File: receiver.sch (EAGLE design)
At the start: 29 parts

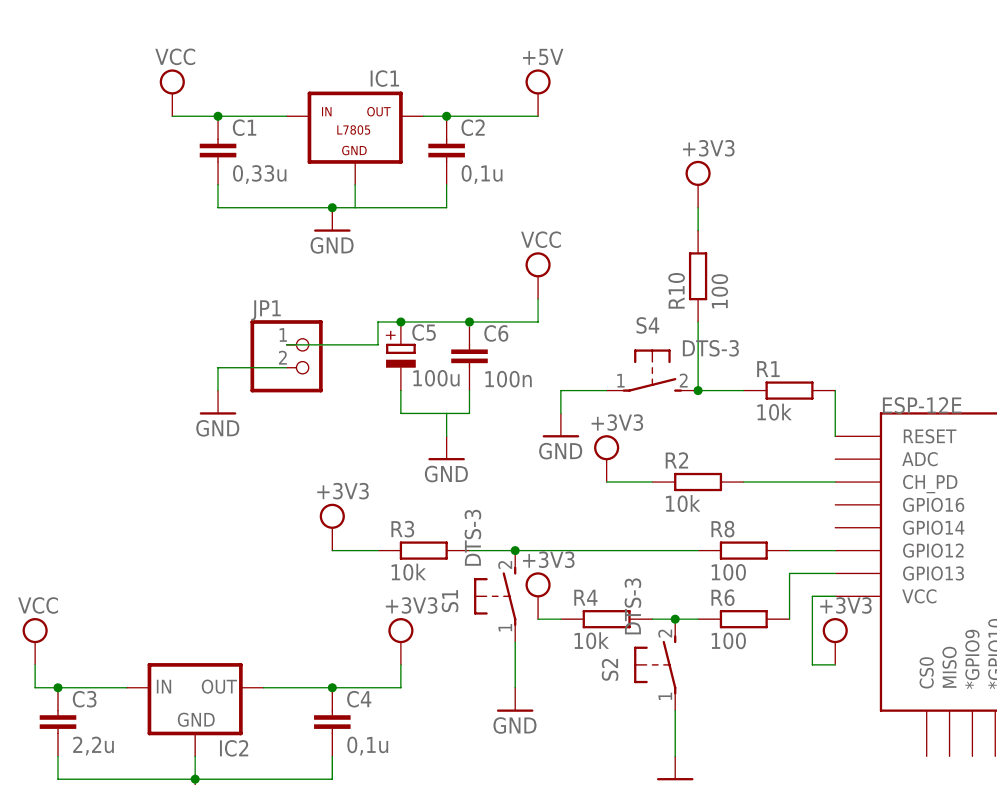
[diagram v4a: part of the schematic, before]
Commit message: Changed 5V LCD on 3,3V LCd, replaced 5V from schematic on 3,3V.
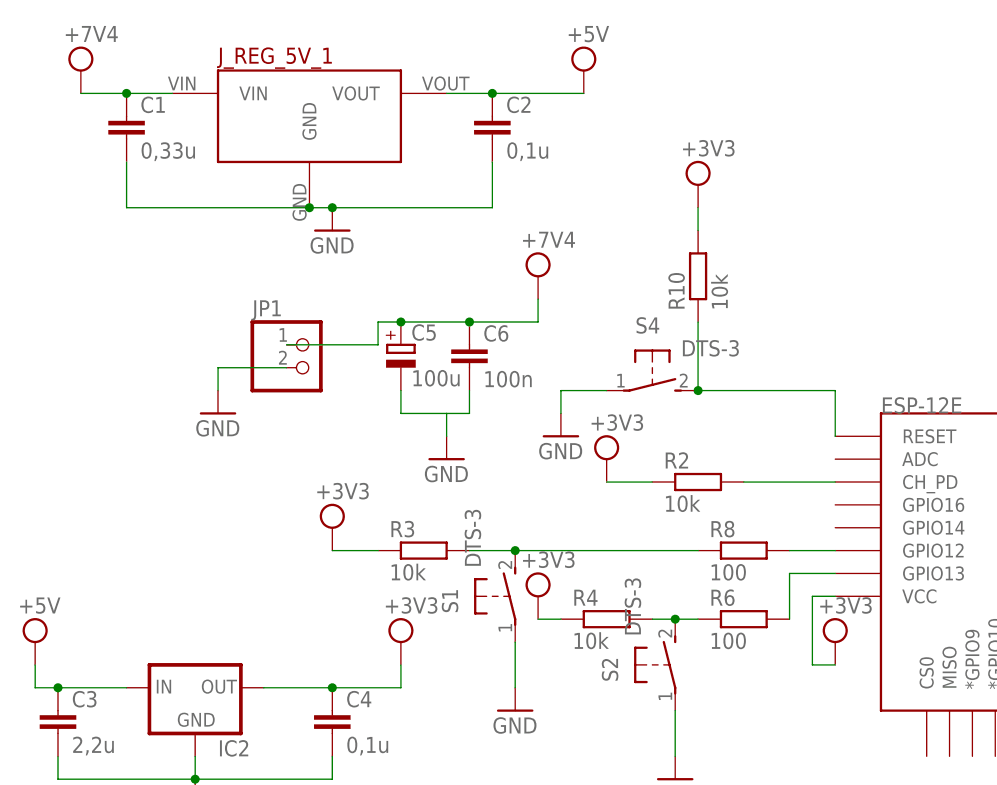
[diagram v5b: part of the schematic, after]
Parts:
- removed IC1: (no value), tango:L7805
- removed R1: 10k, rcl:R-EU_0204/5
- added J_REG_5V_1: 5V_VOLTAGE_REGULATOR, Pololu Voltage Regulators:5V_VOLTAGE_REGULATOR
- R10: value 100 -> 10k
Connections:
- removed net N$12: R1.1, R10.1, S4.2
- net GND: now also J_REG_5V_1.GND; no longer IC1.GND
- net N$1: now also R10.1, S4.2; no longer R1.2
- net VCC: now also J_REG_5V_1.VIN, J_REG_5V_1.VOUT; no longer IC1.IN, IC1.OUT
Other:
- moved on the sheet: C1, C2
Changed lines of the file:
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@@
 <part name="ESP-12E" library="esp8266modules" deviceset="ESP12E" device="SMD"/>
 <part name="GND1" library="supply1" library_urn="urn:adsk.eagle:library:371" deviceset="GND" device=""/>
-<part name="R1" library="rcl" library_urn="urn:adsk.eagle:library:334" deviceset="R-EU_" device="0204/5" package3d_urn="urn:adsk.eagle:package:23488/1" value="10k"/>
 <part name="R2" library="rcl" library_urn="urn:adsk.eagle:library:334" deviceset="R-EU_" device="0204/5" package3d_urn="urn:adsk.eagle:package:23488/1" value="10k"/>
 <part name="LCD" library="pinhead" library_urn="urn:adsk.eagle:library:325" deviceset="PINHD-1X4" device="" package3d_urn="urn:adsk.eagle:package:22407/2"/>
@@
 <part name="R4" library="rcl" library_urn="urn:adsk.eagle:library:334" deviceset="R-EU_" device="0204/5" package3d_urn="urn:adsk.eagle:package:23488/1" value="10k"/>
 <part name="R5" library="rcl" library_urn="urn:adsk.eagle:library:334" deviceset="R-EU_" device="0204/5" package3d_urn="urn:adsk.eagle:package:23488/1" value="10k"/>
-<part name="IC1" library="tango" deviceset="L7805" device=""/>
 <part name="C1" library="rcl" library_urn="urn:adsk.eagle:library:334" deviceset="C-EU" device="025-025X050" package3d_urn="urn:adsk.eagle:package:23629/2" value="0,33u"/>
 <part name="C2" library="rcl" library_urn="urn:adsk.eagle:library:334" deviceset="C-EU" device="025-025X050" package3d_urn="urn:adsk.eagle:package:23629/2" value="0,1u"/>
@@
 <part name="JP1" library="pinhead" library_urn="urn:adsk.eagle:library:325" deviceset="PINHD-1X2" device="" package3d_urn="urn:adsk.eagle:package:22435/2"/>
 <part name="GND6" library="supply1" library_urn="urn:adsk.eagle:library:371" deviceset="GND" device=""/>
-<part name="SUPPLY9" library="supply2" library_urn="urn:adsk.eagle:library:372" deviceset="VCC" device=""/>
+<part name="SUPPLY9" library="supply2" library_urn="urn:adsk.eagle:library:372" deviceset="VCC" device="" value="+7V4"/>
 <part name="IC2" library="lf33" deviceset="LFXXCV" device="L"/>
 <part name="C3" library="rcl" library_urn="urn:adsk.eagle:library:334" deviceset="C-EU" device="025-025X050" package3d_urn="urn:adsk.eagle:package:23629/2" value="2,2u"/>
 <part name="C4" library="rcl" library_urn="urn:adsk.eagle:library:334" deviceset="C-EU" device="025-025X050" package3d_urn="urn:adsk.eagle:package:23629/2" value="0,1u"/>
 <part name="GND7" library="supply1" library_urn="urn:adsk.eagle:library:371" deviceset="GND" device=""/>
-<part name="SUPPLY10" library="supply2" library_urn="urn:adsk.eagle:library:372" deviceset="VCC" device=""/>
+<part name="SUPPLY10" library="supply2" library_urn="urn:adsk.eagle:library:372" deviceset="VCC" device="" value="+5V"/>
 <part name="R6" library="rcl" library_urn="urn:adsk.eagle:library:334" deviceset="R-EU_" device="0204/5" package3d_urn="urn:adsk.eagle:package:23488/1" value="100"/>
 <part name="C5" library="rcl" library_urn="urn:adsk.eagle:library:334" deviceset="CPOL-EU" device="E2.5-6" package3d_urn="urn:adsk.eagle:package:23349/1" value="100u"/>
 <part name="C6" library="rcl" library_urn="urn:adsk.eagle:library:334" deviceset="C-EU" device="025-025X050" package3d_urn="urn:adsk.eagle:package:23629/2" value="100n"/>
-<part name="SUPPLY3" library="supply2" library_urn="urn:adsk.eagle:library:372" deviceset="VCC" device=""/>
+<part name="SUPPLY3" library="supply2" library_urn="urn:adsk.eagle:library:372" deviceset="VCC" device="" value="+7V4"/>
 <part name="GND8" library="supply1" library_urn="urn:adsk.eagle:library:371" deviceset="GND" device=""/>
 <part name="R7" library="rcl" library_urn="urn:adsk.eagle:library:334" deviceset="R-EU_" device="0204/5" package3d_urn="urn:adsk.eagle:package:23488/1" value="10k"/>
@@
 <part name="SUPPLY16" library="supply2" library_urn="urn:adsk.eagle:library:372" deviceset="VCC" device="" value="+3V3"/>
 <part name="S4" library="switch-tact" deviceset="DTS-3" device=""/>
-<part name="R10" library="rcl" library_urn="urn:adsk.eagle:library:334" deviceset="R-EU_" device="0204/5" package3d_urn="urn:adsk.eagle:package:23488/1" value="100"/>
+<part name="R10" library="rcl" library_urn="urn:adsk.eagle:library:334" deviceset="R-EU_" device="0204/5" package3d_urn="urn:adsk.eagle:package:23488/1" value="10k"/>
 <part name="GND9" library="supply1" library_urn="urn:adsk.eagle:library:371" deviceset="GND" device=""/>
 <part name="R11" library="rcl" library_urn="urn:adsk.eagle:library:334" deviceset="R-EU_" device="0204/5" package3d_urn="urn:adsk.eagle:package:23488/1" value="4,7k"/>
@@
 <part name="SUPPLY17" library="supply2" library_urn="urn:adsk.eagle:library:372" deviceset="VCC" device="" value="+5V"/>
 <part name="SUPPLY18" library="supply2" library_urn="urn:adsk.eagle:library:372" deviceset="VCC" device="" value="+5V"/>
+<part name="J_REG_5V_1" library="Pololu Voltage Regulators" deviceset="5V_VOLTAGE_REGULATOR" device=""/>
 </parts>
 <sheets>
@@
 <instance part="ESP-12E" gate="G$1" x="58.42" y="66.04"/>
 <instance part="GND1" gate="1" x="76.2" y="50.8"/>
-<instance part="R1" gate="G$1" x="35.56" y="78.74"/>
 <instance part="R2" gate="G$1" x="25.4" y="68.58"/>
 <instance part="LCD" gate="A" x="152.4" y="73.66"/>
@@
 <instance part="R4" gate="G$1" x="15.24" y="53.34"/>
 <instance part="R5" gate="G$1" x="91.44" y="35.56"/>
-<instance part="IC1" gate="A" x="-12.7" y="106.68"/>
-<instance part="C1" gate="G$1" x="-27.94" y="106.68"/>
-<instance part="C2" gate="G$1" x="-2.54" y="106.68"/>
+<instance part="C1" gate="G$1" x="-38.1" y="109.22"/>
+<instance part="C2" gate="G$1" x="2.54" y="109.22"/>
 <instance part="GND5" gate="1" x="-15.24" y="96.52"/>
 <instance part="JP1" gate="G$1" x="-17.78" y="81.28"/>
 <instance part="GND6" gate="1" x="-27.94" y="76.2"/>
-<instance part="SUPPLY9" gate="G$1" x="-33.02" y="111.76"/>
+<instance part="SUPPLY9" gate="G$1" x="-43.18" y="114.3"/>
 <instance part="IC2" gate="A" x="-30.48" y="45.72"/>
 <instance part="C3" gate="G$1" x="-45.72" y="43.18"/>
@@
 <instance part="SUPPLY8" gate="G$1" x="25.4" y="101.6"/>
 <instance part="SUPPLY11" gate="G$1" x="15.24" y="71.12"/>
-<instance part="SUPPLY12" gate="G$1" x="7.62" y="111.76"/>
+<instance part="SUPPLY12" gate="G$1" x="12.7" y="114.3"/>
 <instance part="SUPPLY7" gate="G$1" x="142.24" y="86.36"/>
 <instance part="SUPPLY4" gate="G$1" x="-15.24" y="63.5"/>
@@
 <instance part="SUPPLY17" gate="G$1" x="134.62" y="99.06"/>
 <instance part="SUPPLY18" gate="G$1" x="134.62" y="55.88"/>
+<instance part="J_REG_5V_1" gate="J_REG_5V" x="-17.78" y="111.76"/>
 </instances>
 <busses>
@@
 <segment>
 <pinref part="C1" gate="G$1" pin="1"/>
-<pinref part="IC1" gate="A" pin="IN"/>
-<wire x1="-27.94" y1="109.22" x2="-20.32" y2="109.22" width="0.1524" layer="91"/>
-<wire x1="-27.94" y1="109.22" x2="-33.02" y2="109.22" width="0.1524" layer="91"/>
-<junction x="-27.94" y="109.22"/>
+<wire x1="-38.1" y1="111.76" x2="-43.18" y2="111.76" width="0.1524" layer="91"/>
 <pinref part="SUPPLY9" gate="G$1" pin="VCC"/>
+<pinref part="J_REG_5V_1" gate="J_REG_5V" pin="VIN"/>
+<wire x1="-33.02" y1="111.76" x2="-38.1" y2="111.76" width="0.1524" layer="91"/>
+<junction x="-38.1" y="111.76"/>
 </segment>
 <segment>
@@
 </segment>
 <segment>
-<pinref part="IC1" gate="A" pin="OUT"/>
-<wire x1="-5.08" y1="109.22" x2="-2.54" y2="109.22" width="0.1524" layer="91"/>
 <pinref part="C2" gate="G$1" pin="1"/>
-<wire x1="-2.54" y1="109.22" x2="7.62" y2="109.22" width="0.1524" layer="91"/>
-<junction x="-2.54" y="109.22"/>
+<wire x1="2.54" y1="111.76" x2="12.7" y2="111.76" width="0.1524" layer="91"/>
 <pinref part="SUPPLY12" gate="G$1" pin="VCC"/>
+<pinref part="J_REG_5V_1" gate="J_REG_5V" pin="VOUT"/>
+<wire x1="-2.54" y1="111.76" x2="2.54" y2="111.76" width="0.1524" layer="91"/>
+<junction x="2.54" y="111.76"/>
 </segment>
 <segment>
@@
 </segment>
 <segment>
-<pinref part="IC1" gate="A" pin="GND"/>
-<wire x1="-12.7" y1="101.6" x2="-12.7" y2="99.06" width="0.1524" layer="91"/>
-<wire x1="-12.7" y1="99.06" x2="-15.24" y2="99.06" width="0.1524" layer="91"/>
-<wire x1="-15.24" y1="99.06" x2="-27.94" y2="99.06" width="0.1524" layer="91"/>
-<wire x1="-12.7" y1="99.06" x2="-2.54" y2="99.06" width="0.1524" layer="91"/>
+<wire x1="-15.24" y1="99.06" x2="-17.78" y2="99.06" width="0.1524" layer="91"/>
+<wire x1="-17.78" y1="99.06" x2="-38.1" y2="99.06" width="0.1524" layer="91"/>
 <pinref part="C1" gate="G$1" pin="2"/>
-<wire x1="-27.94" y1="101.6" x2="-27.94" y2="99.06" width="0.1524" layer="91"/>
+<wire x1="-38.1" y1="104.14" x2="-38.1" y2="99.06" width="0.1524" layer="91"/>
+<pinref part="GND5" gate="1" pin="GND"/>
+<pinref part="J_REG_5V_1" gate="J_REG_5V" pin="GND"/>
+<junction x="-17.78" y="99.06"/>
 <pinref part="C2" gate="G$1" pin="2"/>
-<wire x1="-2.54" y1="101.6" x2="-2.54" y2="99.06" width="0.1524" layer="91"/>
-<pinref part="GND5" gate="1" pin="GND"/>
+<wire x1="-15.24" y1="99.06" x2="2.54" y2="99.06" width="0.1524" layer="91"/>
+<wire x1="2.54" y1="99.06" x2="2.54" y2="104.14" width="0.1524" layer="91"/>
 <junction x="-15.24" y="99.06"/>
 </segment>
@@
 <segment>
 <pinref part="ESP-12E" gate="G$1" pin="RESET"/>
-<pinref part="R1" gate="G$1" pin="2"/>
 <wire x1="40.64" y1="73.66" x2="40.64" y2="78.74" width="0.1524" layer="91"/>
+<pinref part="R10" gate="G$1" pin="1"/>
+<pinref part="S4" gate="G$1" pin="2"/>
+<wire x1="25.4" y1="86.36" x2="25.4" y2="78.74" width="0.1524" layer="91"/>
+<junction x="25.4" y="78.74"/>
+<wire x1="40.64" y1="78.74" x2="25.4" y2="78.74" width="0.1524" layer="91"/>
 </segment>
 </net>
@@
 </segment>
 </net>
-<net name="N$12" class="0">
-<segment>
-<pinref part="R10" gate="G$1" pin="1"/>
-<pinref part="S4" gate="G$1" pin="2"/>
-<wire x1="25.4" y1="86.36" x2="25.4" y2="78.74" width="0.1524" layer="91"/>
-<pinref part="R1" gate="G$1" pin="1"/>
-<wire x1="25.4" y1="78.74" x2="30.48" y2="78.74" width="0.1524" layer="91"/>
-<junction x="25.4" y="78.74"/>
-</segment>
-</net>

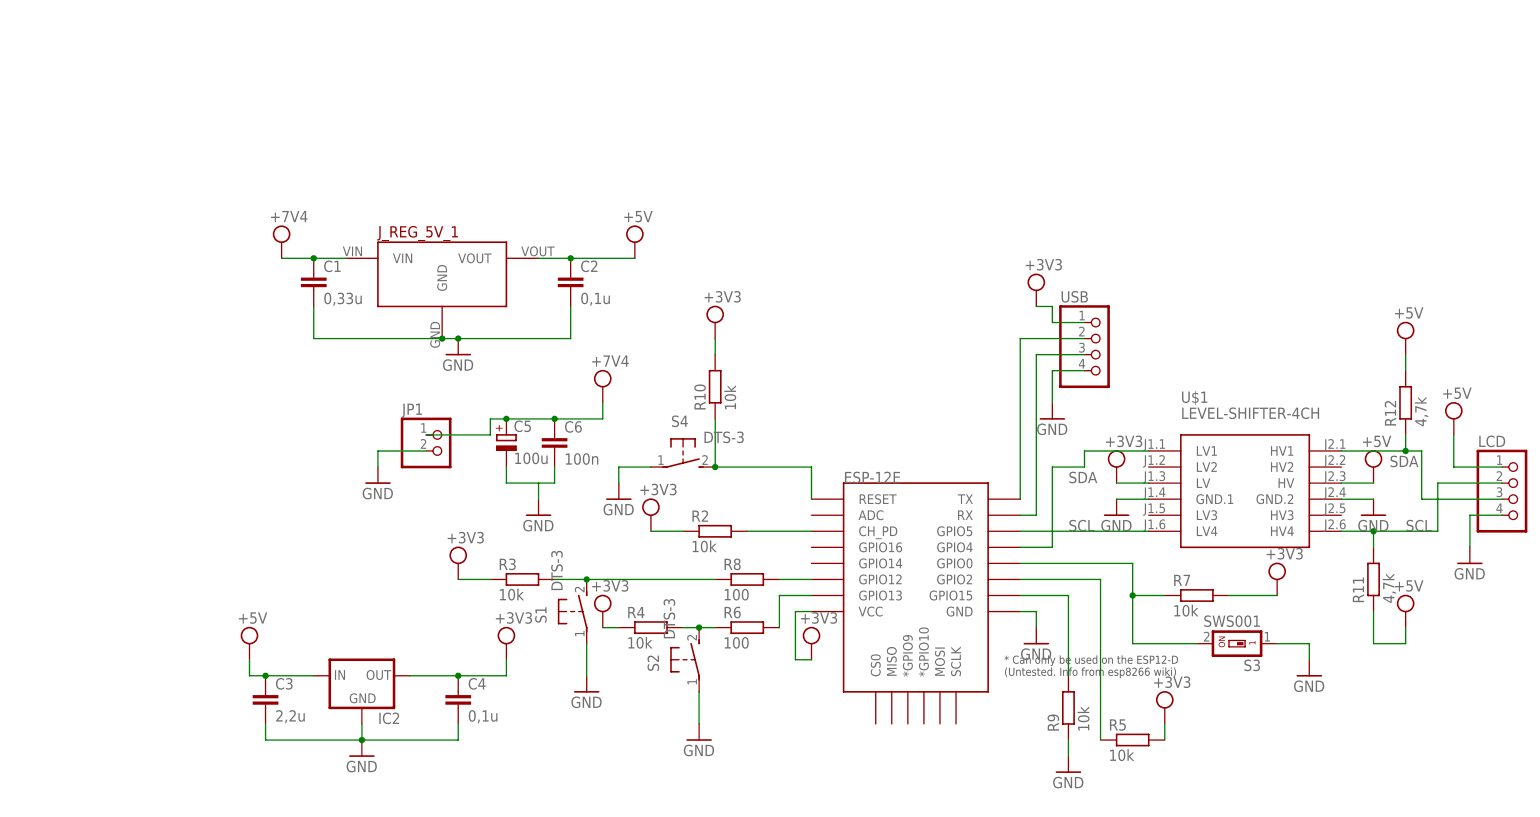
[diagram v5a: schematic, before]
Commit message: Added third button to control device, changed labels of capacitors.
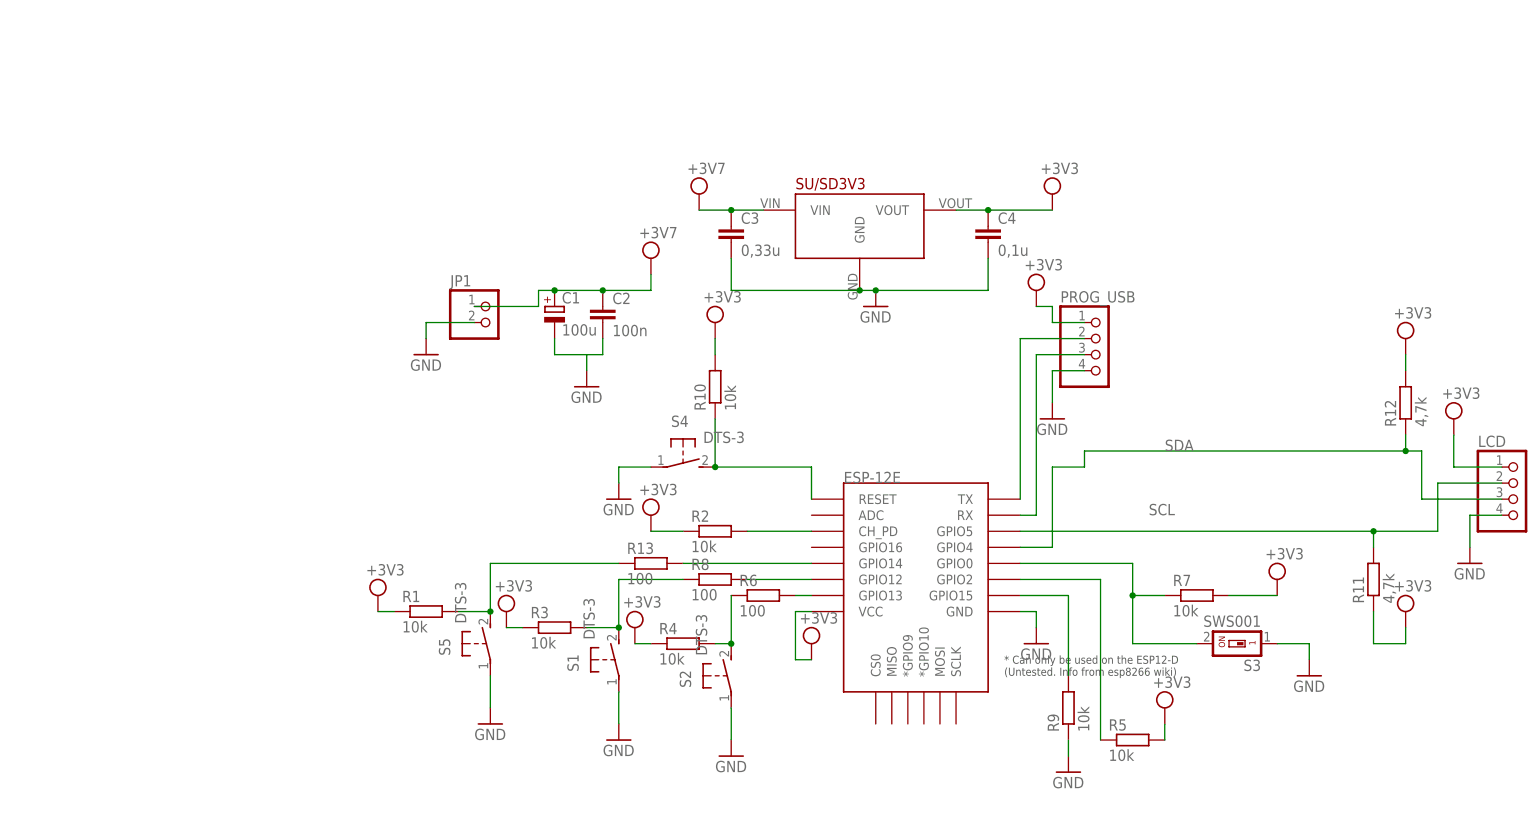
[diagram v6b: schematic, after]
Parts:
- removed C5: 100u, rcl:CPOL-EUE2.5-6
- removed C6: 100n, rcl:C-EU025-025X050
- removed IC2: (no value), lf33:LFXXCVL
- removed J_REG_5V_1: 5V_VOLTAGE_REGULATOR, Pololu Voltage Regulators:5V_VOLTAGE_REGULATOR
- removed U$1: LEVEL-SHIFTER-4CH, diy-modules:LEVEL-SHIFTER-4CH
- added R1: 10k, rcl:R-EU_0204/5
- added R13: 100, rcl:R-EU_0204/5
- added S5: DTS-3, switch-tact:DTS-3
- added SU/SD3V3: 5V_VOLTAGE_REGULATOR, Pololu Voltage Regulators:5V_VOLTAGE_REGULATOR
- C1: value 0,33u -> 100u; device rcl:C-EU025-025X050 -> rcl:CPOL-EUE2.5-6
- C2: value 0,1u -> 100n
- C3: value 2,2u -> 0,33u
- renumbered USB to PROG_USB
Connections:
- new net N$12: ESP-12E.GPIO14, R13.2
- new net N$13: R1.2, R13.1, S5.2
- net GND: now also C1.-, S5.1, SU/SD3V3.GND; no longer C1.2, C5.-, C6.2, IC2.GND, J_REG_5V_1.GND, U$1.GND.1, U$1.GND.2
- net SCL: no longer U$1.HV4, U$1.LV4
- net SDA: no longer U$1.HV1, U$1.LV1
- net VCC: now also C1.+, R1.1, SU/SD3V3.VIN, SU/SD3V3.VOUT; no longer C1.1, C5.+, C6.1, IC2.IN, IC2.OUT, J_REG_5V_1.VIN, J_REG_5V_1.VOUT, U$1.HV, U$1.LV
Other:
- moved on the sheet: C2, C3, C4, JP1, R3, R4, R6, R8, S1, S2
